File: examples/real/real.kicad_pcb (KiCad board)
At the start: 2 copper layers, 4.2 x 14.7 mm, 3 parts

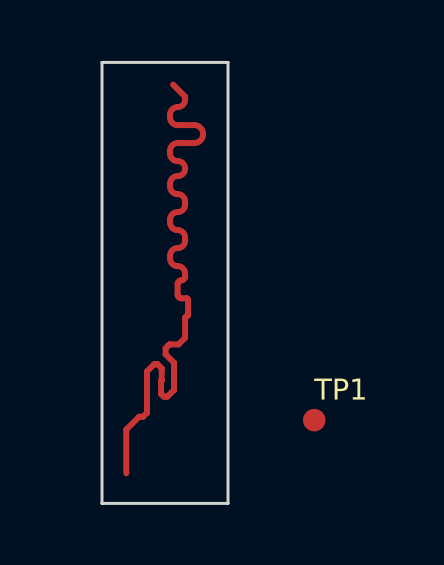
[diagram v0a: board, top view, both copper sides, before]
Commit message: Huge rewrite to enhance functionality and fix some limitations
- Allow for selection of input and output folders.
- Added settings for:
    - Adjusting xy offset of port positions.
    - Settings to control nanomesh quality when converting gerbers to images.
    - Unified 0 indexing for simulation ports in KiCAD schematic and python scripts.
    - Allow adjusting smoothing ratio for mesh lines.
    - Stackup layers moved from separate "fab/stackup.json" to inside "simulation.json".
    - Backup gerber files and simulation.json config inside simulation output to keep track of parametric search changes in schematic.
    - Output visualisation of gerber to image mesh for debugging semi-buggy nanomesh workflow where there will be unwanted merging of nets.
    - Added option for dielectric layers to use a gerber file as mesh.
    - Added option to repeat layer for given z-heights.
- Fixed examples/* to reflect modifications to gerber2ems.
- Added examples/differential_hatched as additional example.
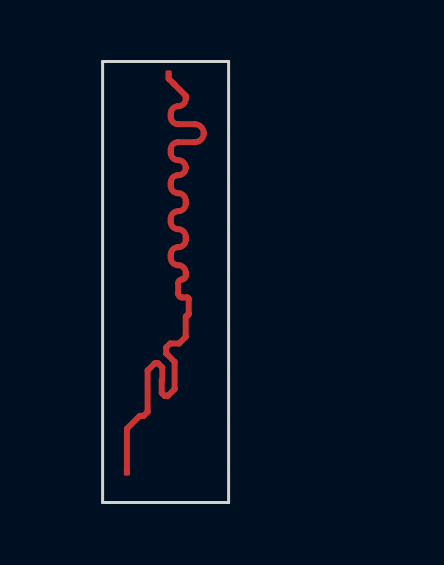
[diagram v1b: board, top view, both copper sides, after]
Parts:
- removed TP1: TP_0.75mm_SMD, antmicro-footprints:TP_SMD_0.75mm
- added SP0: Simulation_Port, NetTie:NetTie-2_SMD_Pad0.5mm, F.Cu at (143.9, 84.3)
- added SP1: Simulation_Port, NetTie:NetTie-2_SMD_Pad0.5mm, F.Cu at (142.5, 97.8)

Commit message: Update examples with corrected settings and keep track of exported gerbers
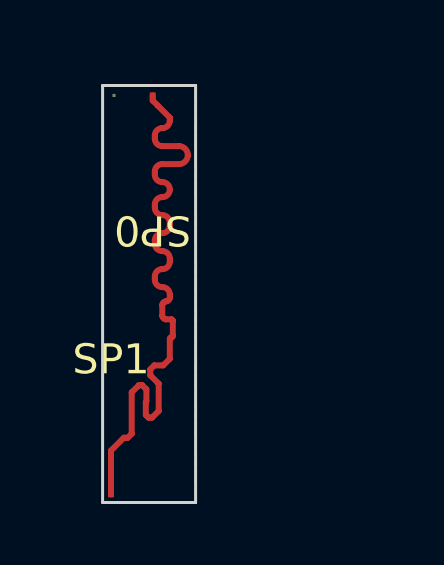
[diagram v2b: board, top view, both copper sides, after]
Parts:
- removed the SP1 at (142.5, 97.8) (x2)
- added GND1: GND, simulation_port:pad_0.1mm, B.Cu at (142.1, 85.1)
- added SP1: Simulation_Port, simulation_port:pad_0.2mm, F.Cu at (142.0, 98.4)
- SP0: footprint NetTie:NetTie-2_SMD_Pad0.5mm -> simulation_port:pad_0.2mm
- moved SP0 0.98 mm to (143.4, 85.1)
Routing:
- added copper zone on B.Cu, net GND
- removed copper zone on B.Cu, net (none)
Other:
- board size 4.2 x 14.7 mm -> 3.1 x 13.9 mm
